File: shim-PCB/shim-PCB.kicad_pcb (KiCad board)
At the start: 2 copper layers, 67.5 x 95.4 mm, 25 parts, among them J1 ROMI-Encoder, J10 LineSensor, J11 LineSensor, J12 SPI, J13 Ultrasonic., J14 THING, J15 THING, J16 Conn_01x02_Female, J17 i2c, J2 ROMI-Encoder, J3 Conn_01x19_Female, J4 ServoAnalog, J5 Conn_01x19_Female, J6 Conn_01x19_Female, J7 ROMI, J8 ROMI, J9 Conn_01x19_Female

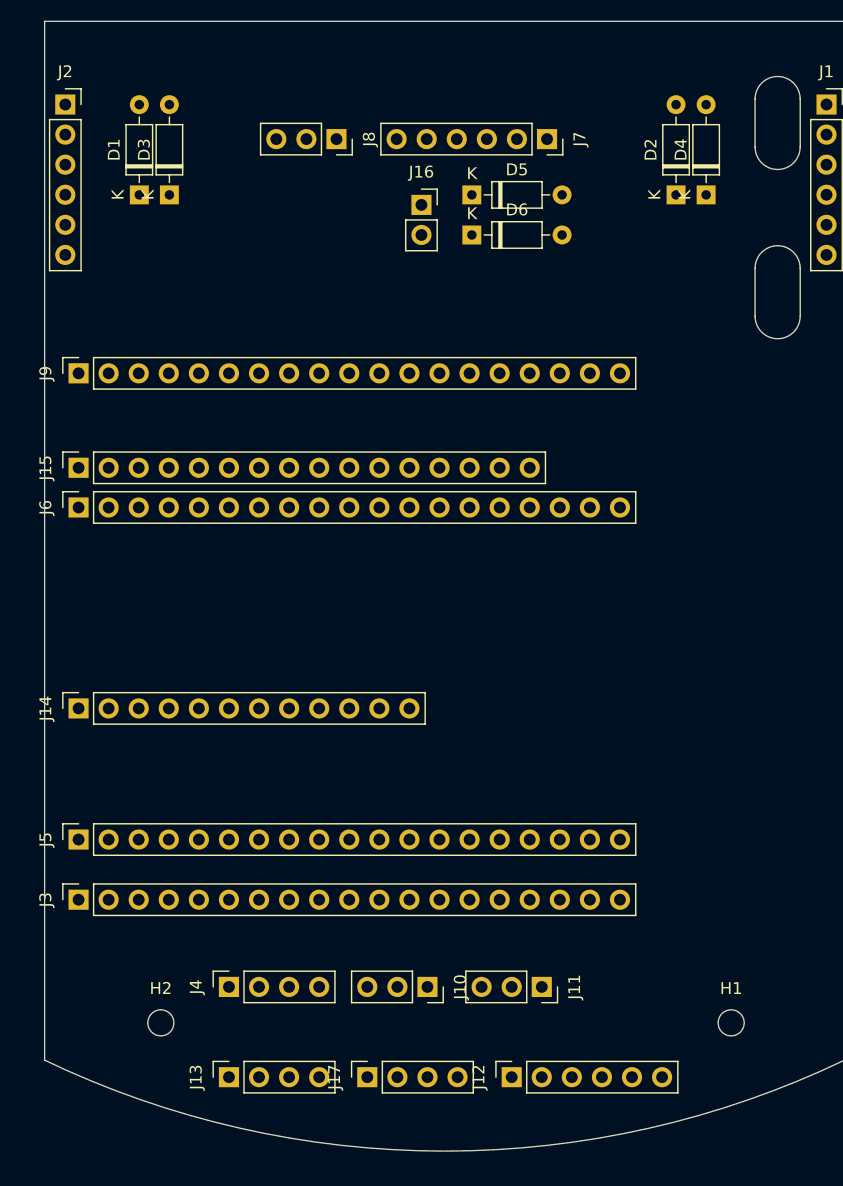
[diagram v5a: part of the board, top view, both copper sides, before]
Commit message: routing power and ground
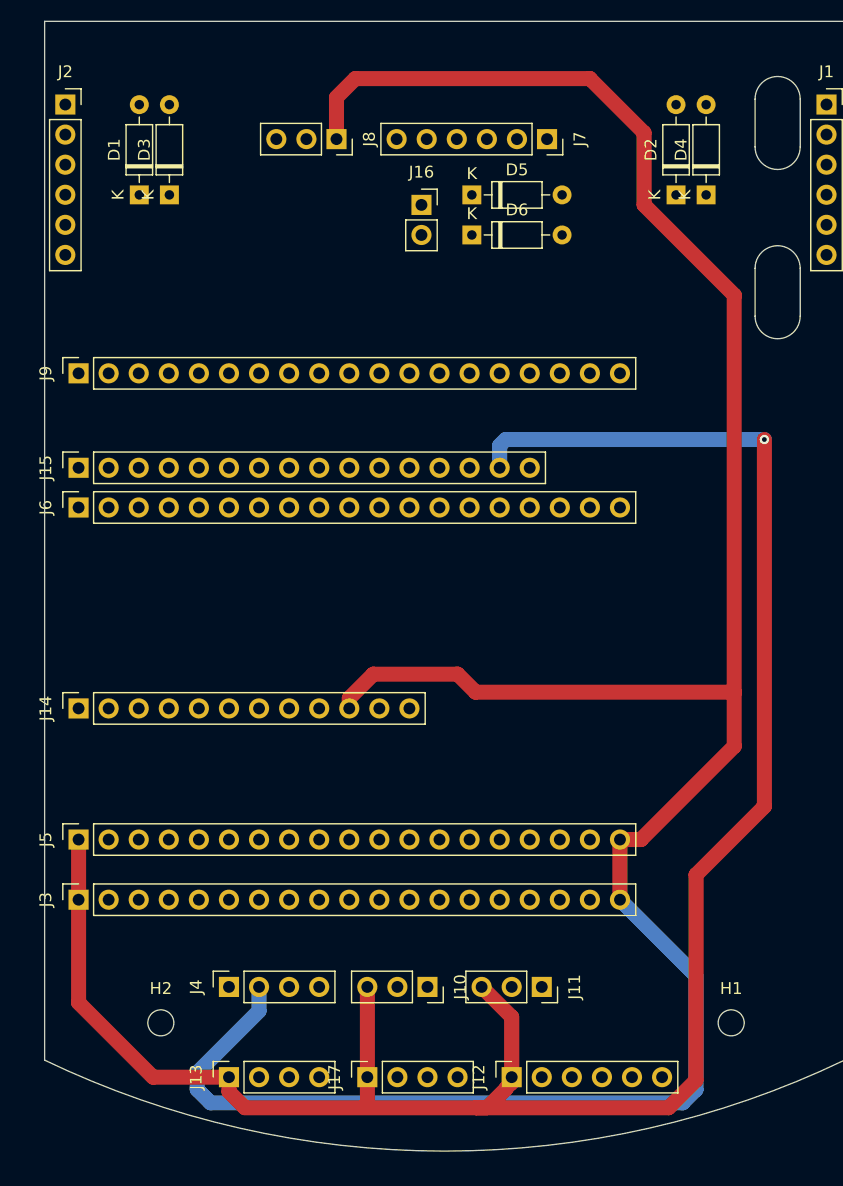
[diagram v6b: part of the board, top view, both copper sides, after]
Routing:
- net +5V: track 0.00 -> 212.4 mm
- net +3V3: track 0.00 -> 175.3 mm, vias 0 -> 1
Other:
- rule trace_min: 0.2 -> 0.1524
- rule via_min_drill: 0.3 -> 0.254
- rule via_min_size: 0.4 -> 0.508
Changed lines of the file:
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@@
     (thickness 1.6)
     (drawings 159)
-    (tracks 0)
+    (tracks 49)
     (zones 0)
     (modules 25)
@@
   )
   (setup
-    (last_trace_width 0.25)
+    (last_trace_width 1.27)
+    (user_trace_width 0.1524)
+    (user_trace_width 0.2032)
+    (user_trace_width 0.3048)
+    (user_trace_width 0.4064)
+    (user_trace_width 0.6096)
+    (user_trace_width 1.27)
     (trace_clearance 0.2)
     (zone_clearance 0.2032)
     (zone_45_only no)
-    (trace_min 0.2)
+    (trace_min 0.1524)
     (via_size 0.8)
     (via_drill 0.4)
-    (via_min_size 0.4)
-    (via_min_drill 0.3)
+    (via_min_size 0.508)
+    (via_min_drill 0.254)
+    (user_via 0.508 0.254)
     (uvia_size 0.3)
     (uvia_drill 0.1)
@@
   (gr_circle (center 125.984 77.724) (end 126.634 77.724) (layer Dwgs.User) (width 0.05))
   (gr_circle (center 115.824 122.174) (end 116.474 122.174) (layer Dwgs.User) (width 0.05))
+  (segment (start 132.525 57.9444) (end 132.525 54.419) (width 1.27) (layer F.Cu) (net 24))
+  (segment (start 132.525 54.419) (end 134.112 52.832) (width 1.27) (layer F.Cu) (net 24))
+  (segment (start 134.112 52.832) (end 153.924 52.832) (width 1.27) (layer F.Cu) (net 24))
+  (segment (start 153.924 52.832) (end 158.496 57.404) (width 1.27) (layer F.Cu) (net 24))
+  (segment (start 158.496 57.404) (end 158.496 63.5) (width 1.27) (layer F.Cu) (net 24))
+  (segment (start 158.496 63.5) (end 166.116 71.12) (width 1.27) (layer F.Cu) (net 24))
+  (segment (start 166.116 71.12) (end 166.116 104.648) (width 1.27) (layer F.Cu) (net 24))
+  (segment (start 166.116 104.648) (end 144.272 104.648) (width 1.27) (layer F.Cu) (net 24))
+  (segment (start 144.272 104.648) (end 142.748 103.124) (width 1.27) (layer F.Cu) (net 24))
+  (segment (start 142.748 103.124) (end 135.636 103.124) (width 1.27) (layer F.Cu) (net 24))
+  (segment (start 133.604 105.156) (end 133.604 106.02) (width 1.27) (layer F.Cu) (net 24))
+  (segment (start 135.636 103.124) (end 133.604 105.156) (width 1.27) (layer F.Cu) (net 24))
+  (segment (start 156.464 122.174) (end 156.464 117.094) (width 1.27) (layer F.Cu) (net 24))
+  (segment (start 156.464 117.094) (end 158.242 117.094) (width 1.27) (layer F.Cu) (net 24))
+  (segment (start 166.116 109.22) (end 166.116 104.648) (width 1.27) (layer F.Cu) (net 24))
+  (segment (start 158.242 117.094) (end 166.116 109.22) (width 1.27) (layer F.Cu) (net 24))
+  (segment (start 125.984 129.54) (end 125.984 131.572) (width 1.27) (layer B.Cu) (net 24))
+  (segment (start 125.984 131.572) (end 120.761371 136.794629) (width 1.27) (layer B.Cu) (net 24))
+  (segment (start 120.761371 136.794629) (end 120.761371 138.201005) (width 1.27) (layer B.Cu) (net 24))
+  (segment (start 120.761371 138.201005) (end 121.889048 139.328682) (width 1.27) (layer B.Cu) (net 24))
+  (segment (start 121.889048 139.328682) (end 161.762311 139.328682) (width 1.27) (layer B.Cu) (net 24))
+  (segment (start 161.762311 139.328682) (end 162.885771 138.205222) (width 1.27) (layer B.Cu) (net 24))
+  (segment (start 162.885771 128.595771) (end 156.464 122.174) (width 1.27) (layer B.Cu) (net 24))
+  (segment (start 162.885771 138.205222) (end 162.885771 128.595771) (width 1.27) (layer B.Cu) (net 24))
+  (segment (start 123.444 137.16) (end 123.444 138.390887) (width 1.27) (layer F.Cu) (net 34))
+  (segment (start 123.444 138.390887) (end 124.798653 139.74554) (width 1.27) (layer F.Cu) (net 34))
+  (segment (start 145.24246 139.74554) (end 146.812 138.176) (width 1.27) (layer F.Cu) (net 34))
+  (segment (start 147.32 137.621128) (end 146.816944 138.124184) (width 1.27) (layer F.Cu) (net 34))
+  (segment (start 147.32 137.16) (end 147.32 137.621128) (width 1.27) (layer F.Cu) (net 34))
+  (segment (start 135.128 139.482814) (end 135.236665 139.591479) (width 1.27) (layer F.Cu) (net 34))
+  (segment (start 135.128 137.16) (end 135.128 139.482814) (width 1.27) (layer F.Cu) (net 34))
+  (segment (start 135.128 137.16) (end 135.128 129.54) (width 1.27) (layer F.Cu) (net 34))
+  (segment (start 147.32 132.08) (end 144.78 129.54) (width 1.27) (layer F.Cu) (net 34))
+  (segment (start 147.32 137.16) (end 147.32 132.08) (width 1.27) (layer F.Cu) (net 34))
+  (segment (start 144.31754 139.74554) (end 160.564337 139.74554) (width 1.27) (layer F.Cu) (net 34))
+  (segment (start 144.31754 139.74554) (end 145.24246 139.74554) (width 1.27) (layer F.Cu) (net 34))
+  (segment (start 124.798653 139.74554) (end 144.31754 139.74554) (width 1.27) (layer F.Cu) (net 34))
+  (segment (start 160.564337 139.74554) (end 162.885771 137.424106) (width 1.27) (layer F.Cu) (net 34))
+  (segment (start 162.885771 137.424106) (end 162.885771 120.070229) (width 1.27) (layer F.Cu) (net 34))
+  (segment (start 123.444 137.16) (end 117.035648 137.16) (width 1.27) (layer F.Cu) (net 34))
+  (segment (start 110.744 130.868352) (end 110.744 122.174) (width 1.27) (layer F.Cu) (net 34))
+  (segment (start 117.035648 137.16) (end 110.744 130.868352) (width 1.27) (layer F.Cu) (net 34))
+  (segment (start 110.744 122.174) (end 110.744 117.094) (width 1.27) (layer F.Cu) (net 34))
+  (segment (start 146.304 85.7005) (end 146.304 83.82) (width 1.27) (layer B.Cu) (net 34))
+  (segment (start 146.304 83.82) (end 146.812 83.312) (width 1.27) (layer B.Cu) (net 34))
+  (via (at 168.656 83.312) (size 0.8) (drill 0.4) (layers F.Cu B.Cu) (net 34))
+  (segment (start 146.812 83.312) (end 168.656 83.312) (width 1.27) (layer B.Cu) (net 34))
+  (segment (start 168.656 114.3) (end 162.885771 120.070229) (width 1.27) (layer F.Cu) (net 34))
+  (segment (start 168.656 83.312) (end 168.656 114.3) (width 1.27) (layer F.Cu) (net 34))
   (zone (net 1) (net_name GND) (layer B.Cu) (hatch edge 0.508)
     (connect_pads (clearance 0.2032))

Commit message: Finished routing
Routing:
- net GPIO27: track 0.00 -> 132.4 mm, vias 0 -> 3
- net GPIO21: track 0.00 -> 112.7 mm
- net GPIO15: track 0.00 -> 112.1 mm, vias 0 -> 1
- net GPIO34: track 0.00 -> 106.1 mm, vias 0 -> 1
- net GPIO19: track 0.00 -> 105.9 mm, vias 0 -> 8
- net GPIO18: track 0.00 -> 99.7 mm, vias 0 -> 7
- net GPIO5: track 0.00 -> 95.8 mm, vias 0 -> 7
- net GPIO23: track 0.00 -> 91.2 mm, vias 0 -> 1
- net GPIO26: track 0.00 -> 88.3 mm, vias 0 -> 2
- net GPIO22: track 0.00 -> 86.5 mm, vias 0 -> 2
- net GPIO13: track 0.00 -> 85.9 mm
- net GPIO16: track 0.00 -> 81.6 mm, vias 0 -> 2
- net GPIO12: track 0.00 -> 80.4 mm, vias 0 -> 1
- net GPIO25: track 0.00 -> 78.8 mm, vias 0 -> 6
- net GPIO39: track 0.00 -> 73.7 mm, vias 0 -> 1
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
